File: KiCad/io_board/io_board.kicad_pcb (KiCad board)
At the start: 4 copper layers, 160.3 x 99.1 mm, 78 parts, among them J1 RS232, J2 Mini-DIN-6, J3 SD_Card, J4 JTAG, J5 DS1307, J6 BME280, U1 ST16C550CJ44, U10 74HC367, U11 74HC367, U12 AMS1117-3.3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

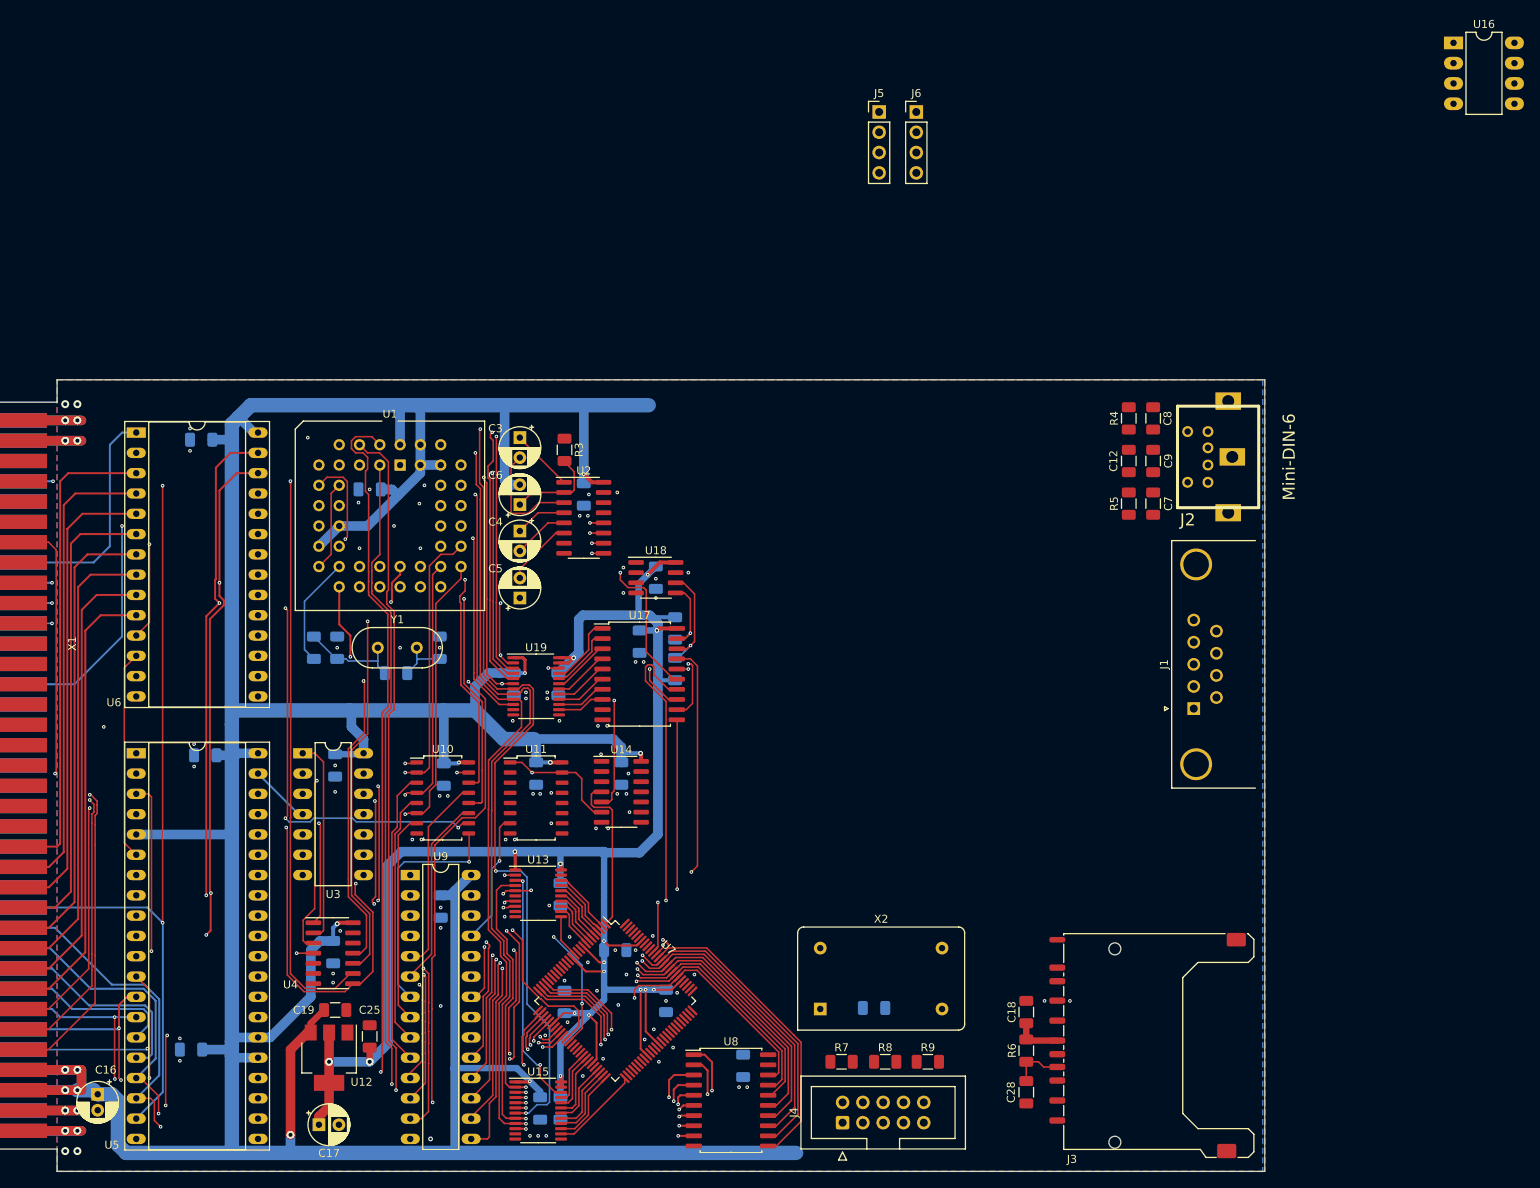
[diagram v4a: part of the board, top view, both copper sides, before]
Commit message: Updated I/O board.
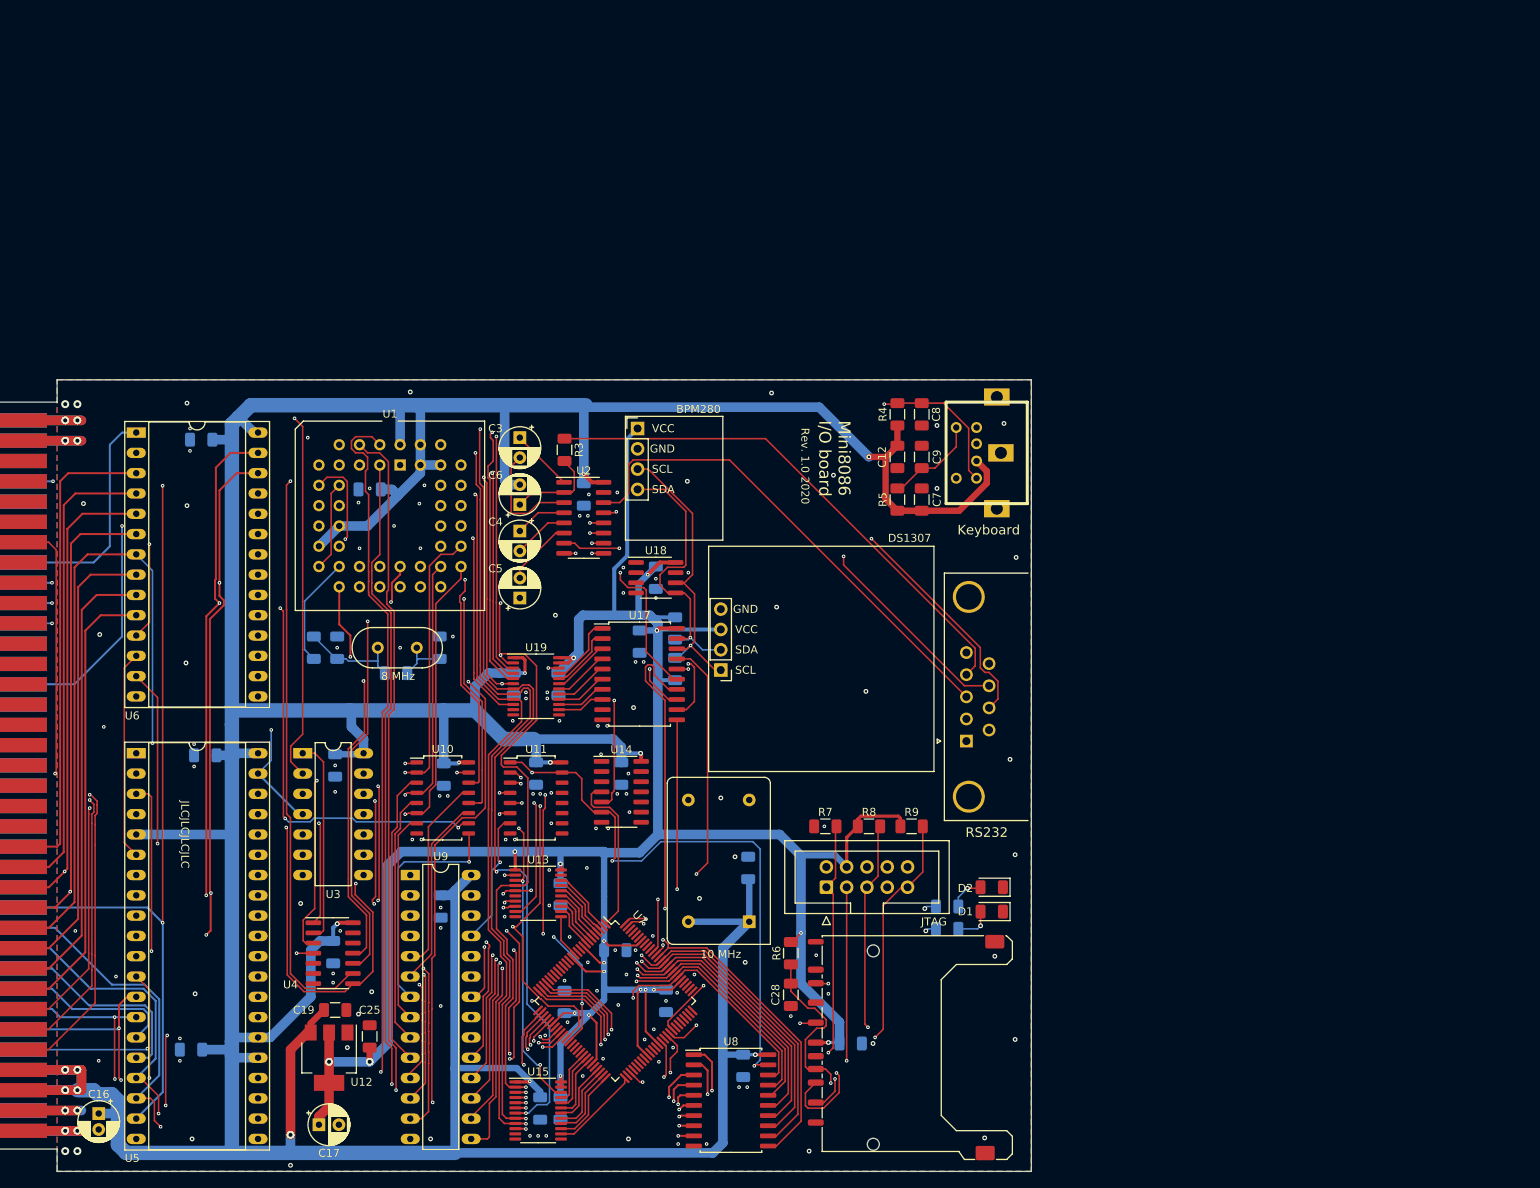
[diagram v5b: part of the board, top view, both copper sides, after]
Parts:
- removed U16: MAX485E, Package_DIP:DIP-8_W7.62mm_LongPads
- added D1: green, LED_SMD:LED_1206_3216Metric, F.Cu at (157.6, 119.9)
- added D2: red, LED_SMD:LED_1206_3216Metric, F.Cu at (157.6, 116.8)
- added R12: 270, Resistor_SMD:R_1206_3216Metric, B.Cu at (152.0, 122.0)
- added R13: 270, Resistor_SMD:R_1206_3216Metric, B.Cu at (152.0, 119.3)
- C18: moved to B.Cu
- J2: value Mini-DIN-6 -> Keyboard
- moved J5 72.6 mm to (123.7, 89.7), turned to 180 degrees
- moved J6 52.8 mm to (113.3, 59.4)
- moved C28 31.9 mm to (132.5, 130.3)
- moved R6 31.9 mm to (132.5, 125.1)
- moved J3 30.2 mm to (148.1, 136.9)
- moved J4 29.5 mm to (136.9, 116.8)
- moved R7 29.5 mm to (136.8, 109.2)
- moved R8 29.5 mm to (142.2, 109.2)
- moved R9 29.5 mm to (147.6, 109.2)
- moved C12 29.0 mm to (145.8, 63.0)
- moved C7 29.0 mm to (148.8, 68.3)
- moved C8 29.0 mm to (148.8, 57.7)
- moved C9 29.0 mm to (148.8, 63.0)
- moved R4 29.0 mm to (145.8, 57.7)
- moved R5 29.0 mm to (145.8, 68.3)
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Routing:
- net /PS2/KBD_DATA: track 8.20 -> 158.5 mm, vias 0 -> 1
- net /PS2/KBD_CLK: track 21.9 -> 161.1 mm, vias 0 -> 2
- net VCC: track 561.9 -> 663.7 mm, vias 12 -> 14
- net VCC3: track 251.6 -> 347.4 mm, vias 16 -> 18
- net A6: track 58.9 -> 137.3 mm, vias 0 -> 2
- net ~CS_DRIVE: track 30.1 -> 105.9 mm, vias 2 -> 4
- net /serial/RTS: track 0.00 -> 67.7 mm, vias 0 -> 2
- net A8: track 59.3 -> 126.8 mm, vias 0 -> 2
- net Net-(J1-Pad4): track 0.00 -> 66.0 mm
- net /serial/RX: track 0.00 -> 64.2 mm, vias 0 -> 1
- net A7: track 59.9 -> 123.7 mm, vias 0 -> 2
- net /SD drive/TDI: track 12.1 -> 75.7 mm, vias 1 -> 2
- net /serial/TX: track 0.00 -> 62.0 mm
- net /serial/CTS: track 0.00 -> 60.9 mm, vias 0 -> 2
- net /SD drive/TCK: track 12.5 -> 71.3 mm, vias 1 -> 2
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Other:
- board size 160.3 x 99.1 mm -> 131.1 x 99.1 mm
- board text added: "10 MHz"
- board text added: "8 MHz"
- board text added: "BPM280"
- board text added: "DS1307"
- board text added: "GND"
- board text added: "JLCJLCJLCJLC"
- board text added: "JTAG"
- board text added: "Mini8086 I/O board"
- board text added: "RS232"
- board text added: "Rev. 1.0 2020"
- board text added: "SCL"
- board text added: "SDA"
- board text added: "VCC"

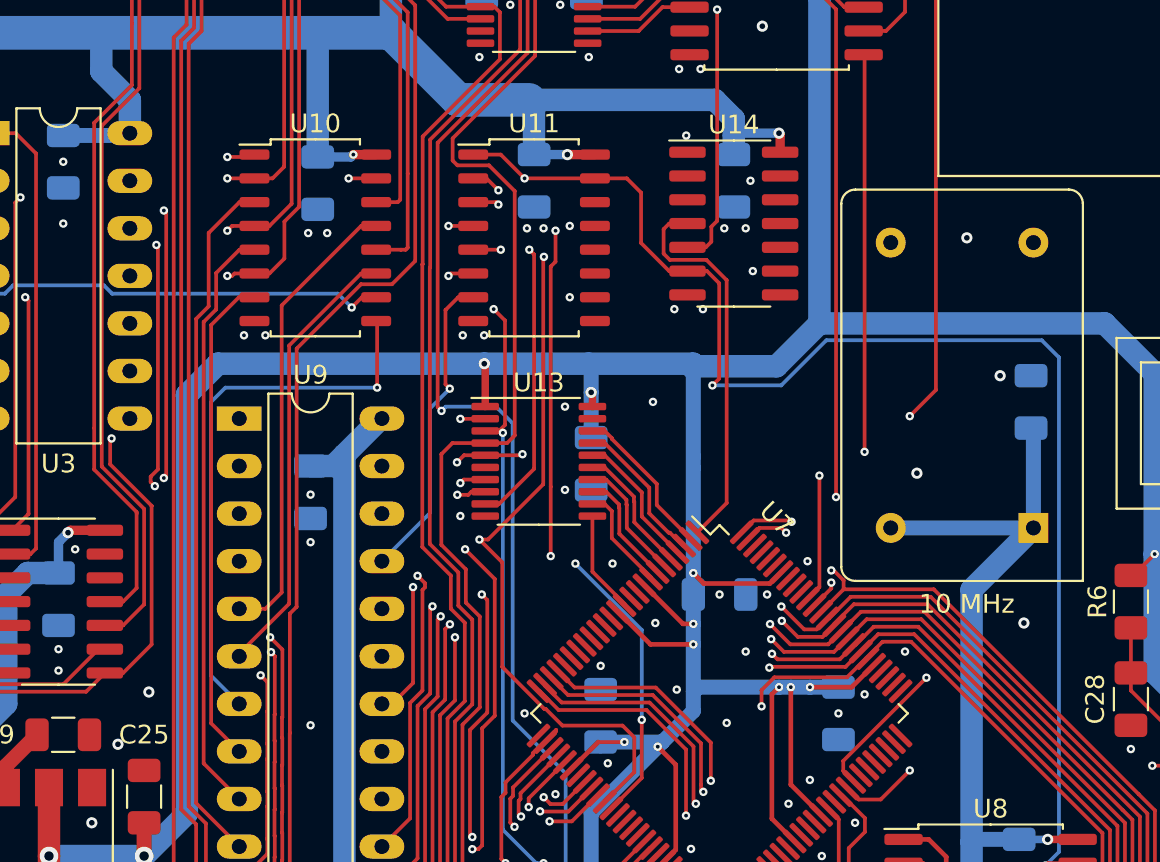
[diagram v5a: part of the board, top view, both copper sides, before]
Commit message: Updated boards (VGA, main, I/O)
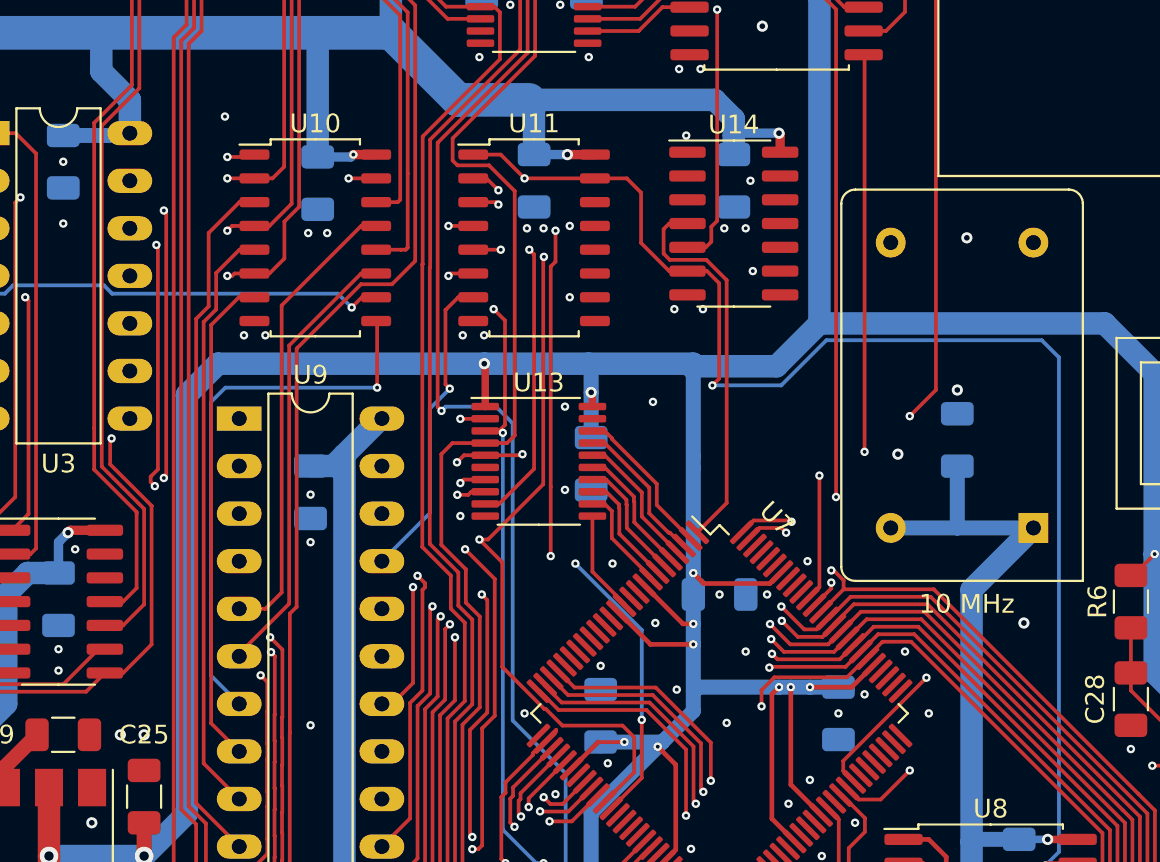
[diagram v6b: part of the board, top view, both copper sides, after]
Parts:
- moved C39 4.43 mm to (123.2, 116.5)
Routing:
- net VCC: track 663.7 -> 661.6 mm
- net GND: vias 149 -> 151

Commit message: Updated I/O board
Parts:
- added C40: 100n, Capacitor_SMD:C_1206_3216Metric, B.Cu at (120.1, 60.8)
- added J7: I²C, Connector_PinHeader_2.54mm:PinHeader_1x04_P2.54mm_Vertical, F.Cu at (127.3, 59.4)
- U3: footprint Package_DIP:DIP-14_W7.62mm_LongPads -> Package_SO:SOIC-14_3.9x8.7mm_P1.27mm
- moved U3 6.17 mm to (75.1, 105.0)
- moved C15 1.30 mm to (75.2, 102.9)
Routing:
- net A0: track 202.4 -> 179.3 mm, vias 6 -> 7
- net SDA: track 36.5 -> 50.4 mm
- net SCL: track 38.5 -> 52.5 mm
- net VCC3: track 347.4 -> 361.4 mm
- net PCLK: track 88.9 -> 85.4 mm
- net /serial/TX: track 62.0 -> 64.9 mm
- net /serial/CTS: track 60.9 -> 63.6 mm
- net Net-(U4-Pad1): track 21.0 -> 18.6 mm
- net ~RESET: track 137.1 -> 134.9 mm
- net Net-(U3-Pad1): track 25.6 -> 23.7 mm
- net Net-(U3-Pad3): track 5.59 -> 7.37 mm, vias 0 -> 1
- net /connector/IRQ7: track 90.1 -> 88.7 mm
- net ~INT_I2C: track 80.1 -> 78.8 mm
- net VCC: track 661.6 -> 662.8 mm, vias 14 -> 15
- net /PS2/KBD_CLK: track 161.1 -> 160.3 mm, vias 2 -> 3
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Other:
- board text added: "I²C"

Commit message: Worked on I/O board.
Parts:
- C3, C4, C5, C6: footprint Capacitor_THT:CP_Radial_D5.0mm_P2.50mm -> Capacitor_SMD:CP_Elec_4x3.9
- moved C3 8.80 mm to (99.3, 69.3)
- moved C5 7.61 mm to (105.9, 78.7), turned to 180 degrees
- moved C6 7.03 mm to (99.3, 62.0)
- moved C4 4.51 mm to (99.3, 76.7)
- moved C34 4.17 mm to (82.3, 70.4), turned to 270 degrees
- turned R2 to 90 degrees
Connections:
- net A11 renamed Net-(X1-Pad16)
- net A12 renamed Net-(X1-Pad17)
- net A13 renamed Net-(X1-Pad18)
- net A14 renamed Net-(X1-Pad19)
- net A15 renamed Net-(X1-Pad20)
- net A16 renamed Net-(X1-Pad21)
- net A17 renamed Net-(X1-Pad22)
- net A18 renamed Net-(X1-Pad23)
- net A19 renamed Net-(X1-Pad24)
- U14 pad 11: Net-(U14-Pad11) -> IRQ6
- U14 pad 12: GND -> SD_IRQ
- U14 pad 13: GND -> SD_IRQ
- U14 pad 5: ~CS_BUFFER -> ~WR_BUFFER
- U5 pad 35: Net-(U5-Pad35) -> IRQ1
- U5 pad 9: Net-(U5-Pad9) -> A0
- U6 pad 15: ~CS_BUFFER -> ~WR_BUFFER
- U7 pad 98: Net-(U7-Pad98) -> SD_IRQ
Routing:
- net IRQ6: track 0.00 -> 97.5 mm, vias 0 -> 2
- net ~WR_BUFFER: track 0.00 -> 84.7 mm, vias 0 -> 3
- net ~CS_BUFFER: track 58.9 -> 0.00 mm, vias 1 -> 0
- net IRQ1: track 0.00 -> 46.5 mm, vias 0 -> 2
- net SD_IRQ: track 0.00 -> 24.7 mm
- net VCC: track 662.8 -> 652.0 mm, vias 15 -> 16
- net Net-(C3-Pad2): track 14.6 -> 5.77 mm
- net Net-(C6-Pad1): track 11.6 -> 17.8 mm
- net A0: track 179.3 -> 184.4 mm, vias 7 -> 8
- net /serial/XTAL2: track 13.8 -> 10.1 mm
- net Net-(C4-Pad2): track 6.98 -> 9.56 mm
- net Net-(C3-Pad1): track 7.88 -> 5.33 mm
- net VCC3: track 361.4 -> 362.8 mm
- net Net-(U1-Pad13): track 37.2 -> 36.1 mm
- net Net-(C2-Pad1): track 12.8 -> 11.8 mm
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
